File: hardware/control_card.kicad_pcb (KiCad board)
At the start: 6 copper layers, 32.5 x 33.8 mm, 144 parts, among them J1 Power board, J2 JTAG, U1 A3CZ065BB18AE7S, U10 SN74LV4051APWR, U11 OPA365AIDBVR, U12 ADS7056IRUGR, U13 SN74LV4051APWR, U14 OPA365AIDBVR, U15 ADS7056IRUGR, U16 TLV75518PDBVR, U2 AP61302Z6-7, U3 AP61102Z6-7, U4 AP61102Z6-7, U5 TLV75512PDBVR, U6 TLV75533PDBVR, U7 MT25QU256ABA8E12-1SIT, U8 SN74AVC4T774RSVR, U9 W958D8NBYA5I, X1 100MHz

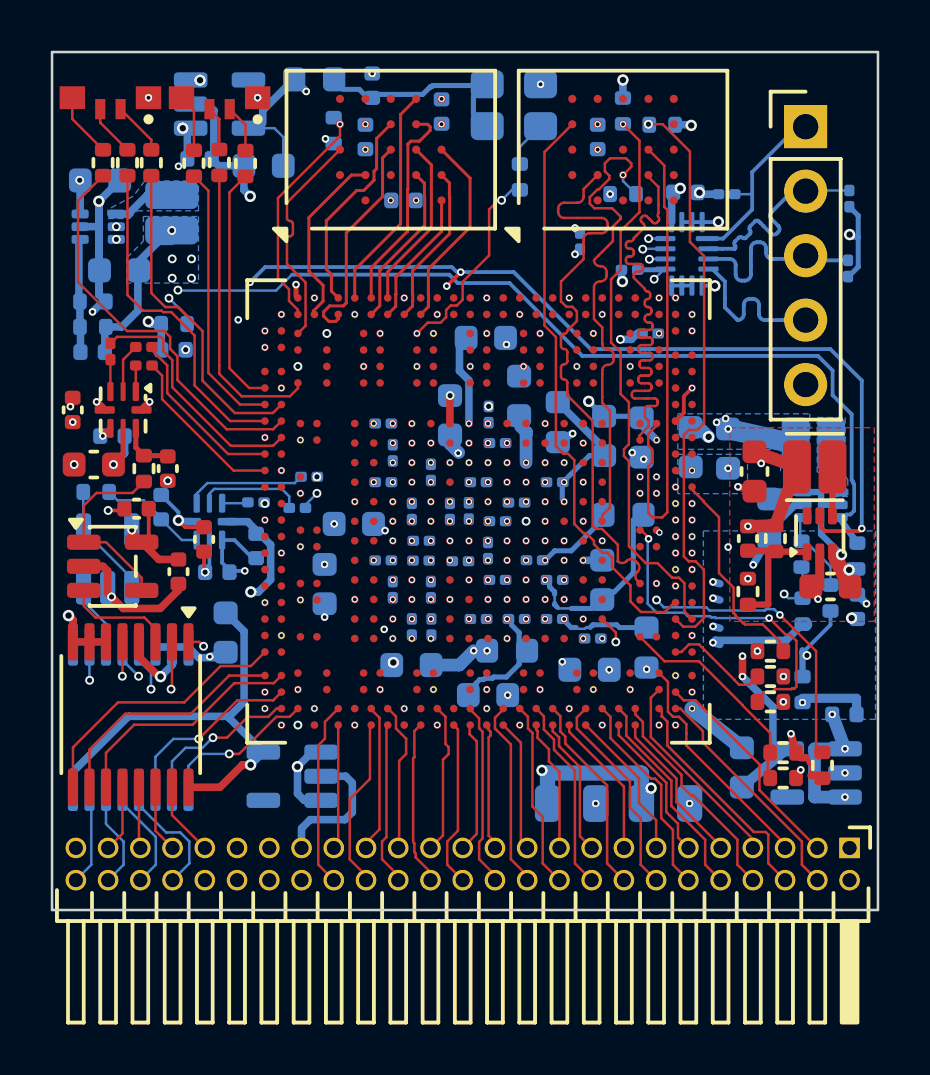
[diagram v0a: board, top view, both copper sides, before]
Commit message: HyperRAM to bank 6D; BGA via-in-pads 0.25/0.15; Default via 0.3/0.15
- Schematic: the 12 HyperRAM signals moved from bank 6C to 6D for easier
  length matching: HR_CK F18 (SOURCE_SYNC_CLK1), CS_N H7, RWDS F10,
  RESET_N F7, DQ0-7 F21 H21 D10 H13 F13 F27 D26 F26. 6D is 1.8 V on
  +1V8_HR and keeps CLK100M on D18; 6C is now unused (No-Connect flags).
  pin_assignment.csv / io_assignment.csv regenerated; docs updated.
- Board: PCB updated from the schematic (HyperRAM reroute in progress);
  ten oversized 0.35/0.2 vias in BGA/0201 pads (incl. U1 D7) reset to
  0.25/0.15 so tracks fit between the balls.
- Default net class via 0.35/0.2 -> 0.3/0.15.

DRC: no clearance errors; 8 unconnected and 9 dangling items, all on the
HyperRAM nets being rerouted.

Co-Authored-By: Claude Opus 5.5 <noreply@anthropic.com>
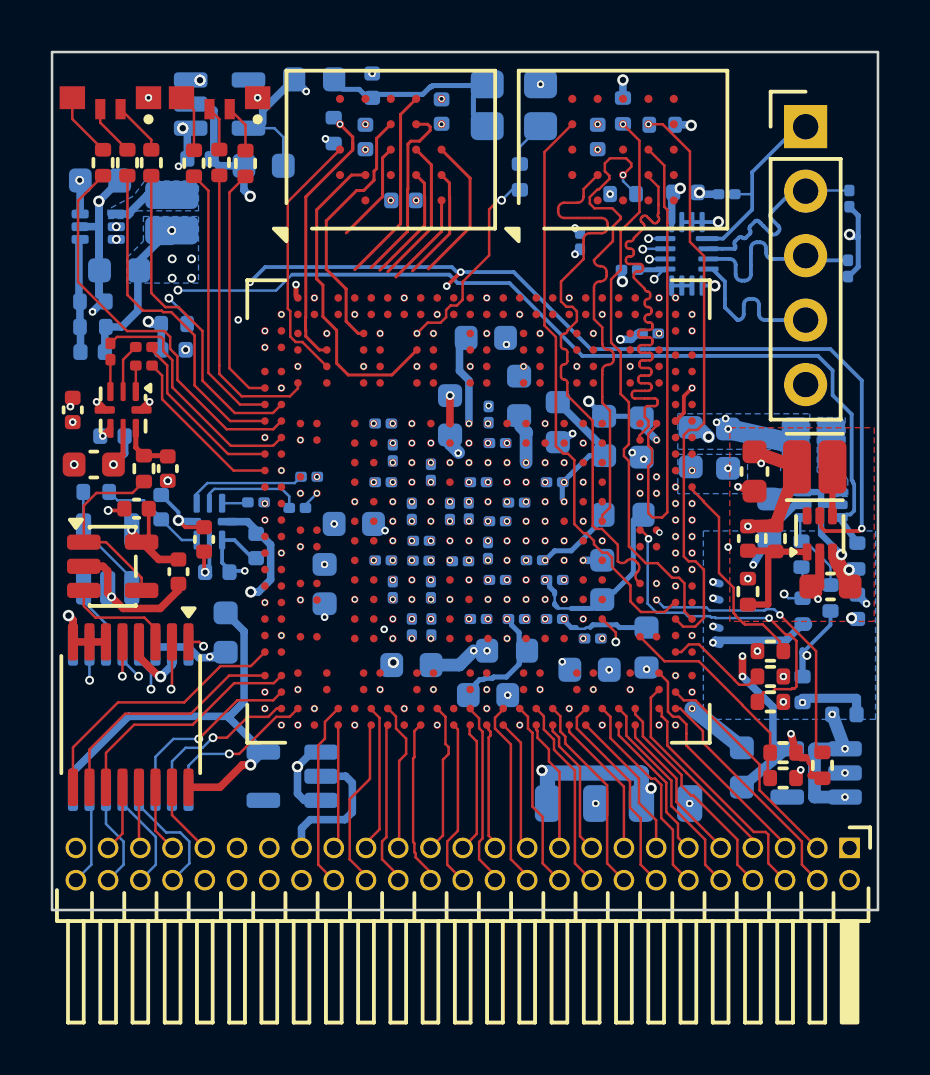
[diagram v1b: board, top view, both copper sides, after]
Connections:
- U1 pad A11: HR_DQ3 -> unconnected-(U1E_6C-6C_IO_HVIO_6C_5_TXCLK5_Data_Ctrl5-PadA11)
- U1 pad A14: HR_DQ0 -> unconnected-(U1E_6C-6C_IO_HVIO_6C_2_TXCLK2_Data_Ctrl2-PadA14)
- U1 pad A8: HR_DQ2 -> unconnected-(U1E_6C-6C_IO_HVIO_6C_9_PLLREFCLK1_TXCLK9_RXCLK1_Data_Ctrl9-PadA8)
- U1 pad A9: HR_DQ4 -> unconnected-(U1E_6C-6C_IO_HVIO_6C_6_TXCLK6_Data_Ctrl6-PadA9)
- U1 pad B11: HR_DQ1 -> unconnected-(U1E_6C-6C_IO_HVIO_6C_7_TXCLK7_Data_Ctrl7-PadB11)
- U1 pad B14: HR_DQ7 -> unconnected-(U1E_6C-6C_IO_HVIO_6C_4_TXCLK4_Data_Ctrl4-PadB14)
- U1 pad B16: HR_DQ6 -> unconnected-(U1E_6C-6C_IO_HVIO_6C_1_TXCLK1_Data_Ctrl1-PadB16)
- U1 pad B19: HR_DQ5 -> unconnected-(U1E_6C-6C_IO_HVIO_6C_3_TXCLK3_Data_Ctrl3-PadB19)
- U1 pad B3: HR_RESET_N -> unconnected-(U1E_6C-6C_IO_HVIO_6C_10_PLLREFCLK2_TXCLK10_RXCLK2_Data_Ctrl10-PadB3)
- U1 pad B5: HR_CK -> unconnected-(U1E_6C-6C_IO_HVIO_6C_11_SOURCE_SYNC_CLK1_TXCLK11_RXCLK3_Data_Ctrl11-PadB5)
- U1 pad B8: HR_RWDS -> unconnected-(U1E_6C-6C_IO_HVIO_6C_8_TXCLK8_Data_Ctrl8-PadB8)
- U1 pad D10: unconnected-(U1F_6D-6D_IO_HVIO_6D_10_PLLREFCLK2_TXCLK10_RXCLK2_Data_Ctrl10-PadD10) -> HR_DQ2
- U1 pad D26: unconnected-(U1F_6D-6D_IO_HVIO_6D_16_TXCLK16_Data_Ctrl16-PadD26) -> HR_DQ6
- U1 pad D3: HR_CS_N -> unconnected-(U1E_6C-6C_IO_HVIO_6C_15_TXCLK15_Data_Ctrl15-PadD3)
- U1 pad F10: unconnected-(U1F_6D-6D_IO_HVIO_6D_4_TXCLK4_Data_Ctrl4-PadF10) -> HR_RWDS
- U1 pad F13: unconnected-(U1F_6D-6D_IO_HVIO_6D_3_TXCLK3_Data_Ctrl3-PadF13) -> HR_DQ4
- U1 pad F18: unconnected-(U1F_6D-6D_IO_HVIO_6D_11_SOURCE_SYNC_CLK1_TXCLK11_RXCLK3_Data_Ctrl11-PadF18) -> HR_CK
- U1 pad F21: unconnected-(U1F_6D-6D_IO_HVIO_6D_12_SOURCE_SYNC_CLK2_TXCLK12_RXCLK4_Data_Ctrl12-PadF21) -> HR_DQ0
- U1 pad F26: unconnected-(U1F_6D-6D_IO_HVIO_6D_18_TXCLK18_Data_Ctrl18-PadF26) -> HR_DQ7
- U1 pad F27: unconnected-(U1F_6D-6D_IO_HVIO_6D_15_TXCLK15_Data_Ctrl15-PadF27) -> HR_DQ5
- U1 pad F7: unconnected-(U1F_6D-6D_IO_HVIO_6D_1_TXCLK1_Data_Ctrl1-PadF7) -> HR_RESET_N
- U1 pad H13: unconnected-(U1F_6D-6D_IO_HVIO_6D_5_TXCLK5_Data_Ctrl5-PadH13) -> HR_DQ3
- U1 pad H21: unconnected-(U1F_6D-6D_IO_HVIO_6D_14_TXCLK14_Data_Ctrl14-PadH21) -> HR_DQ1
- U1 pad H7: unconnected-(U1F_6D-6D_IO_HVIO_6D_2_TXCLK2_Data_Ctrl2-PadH7) -> HR_CS_N
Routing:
- net HR_CK: track 7.14 -> 12.6 mm
- net HR_RWDS: track 8.85 -> 4.01 mm
- net HR_DQ2: track 8.25 -> 10.2 mm
- net HR_DQ5: track 7.77 -> 5.85 mm
- net HR_DQ1: track 6.50 -> 4.62 mm
- net HR_DQ6: track 6.37 -> 4.51 mm
- net HR_RESET_N: track 8.83 -> 10.6 mm
- net HR_DQ7: track 5.37 -> 3.76 mm
- net HR_CS_N: track 8.78 -> 10.2 mm
- net HR_DQ3: track 8.49 -> 7.30 mm
- net HR_DQ4: track 8.84 -> 7.73 mm
- net HR_DQ0: track 6.80 -> 5.77 mm
